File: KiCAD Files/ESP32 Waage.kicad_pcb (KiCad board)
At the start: 2 copper layers, 2 parts, among them J1 Conn_01x19_Female, U1 ESP32-WROVER

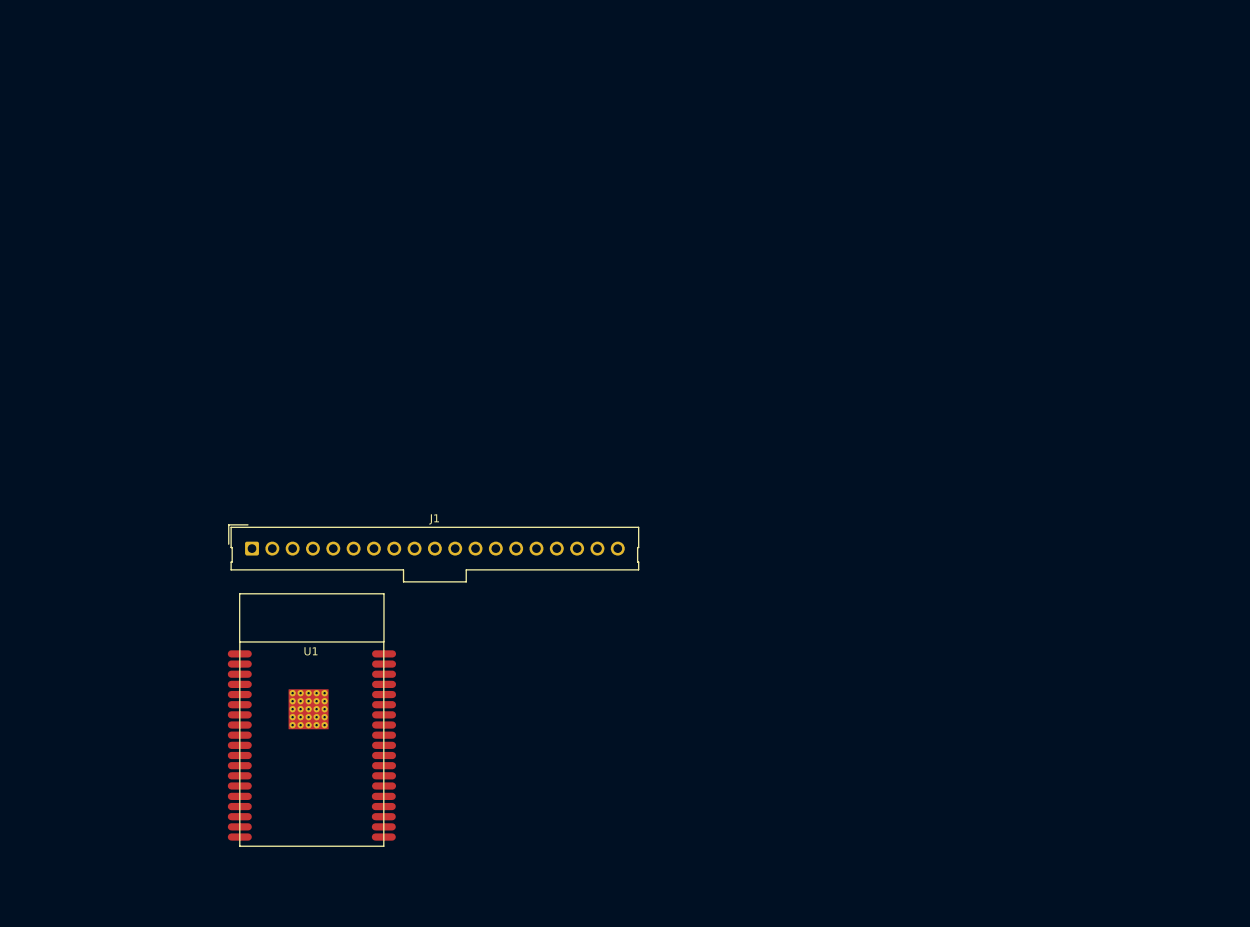
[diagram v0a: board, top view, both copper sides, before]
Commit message: Optocoupler Mounting holes
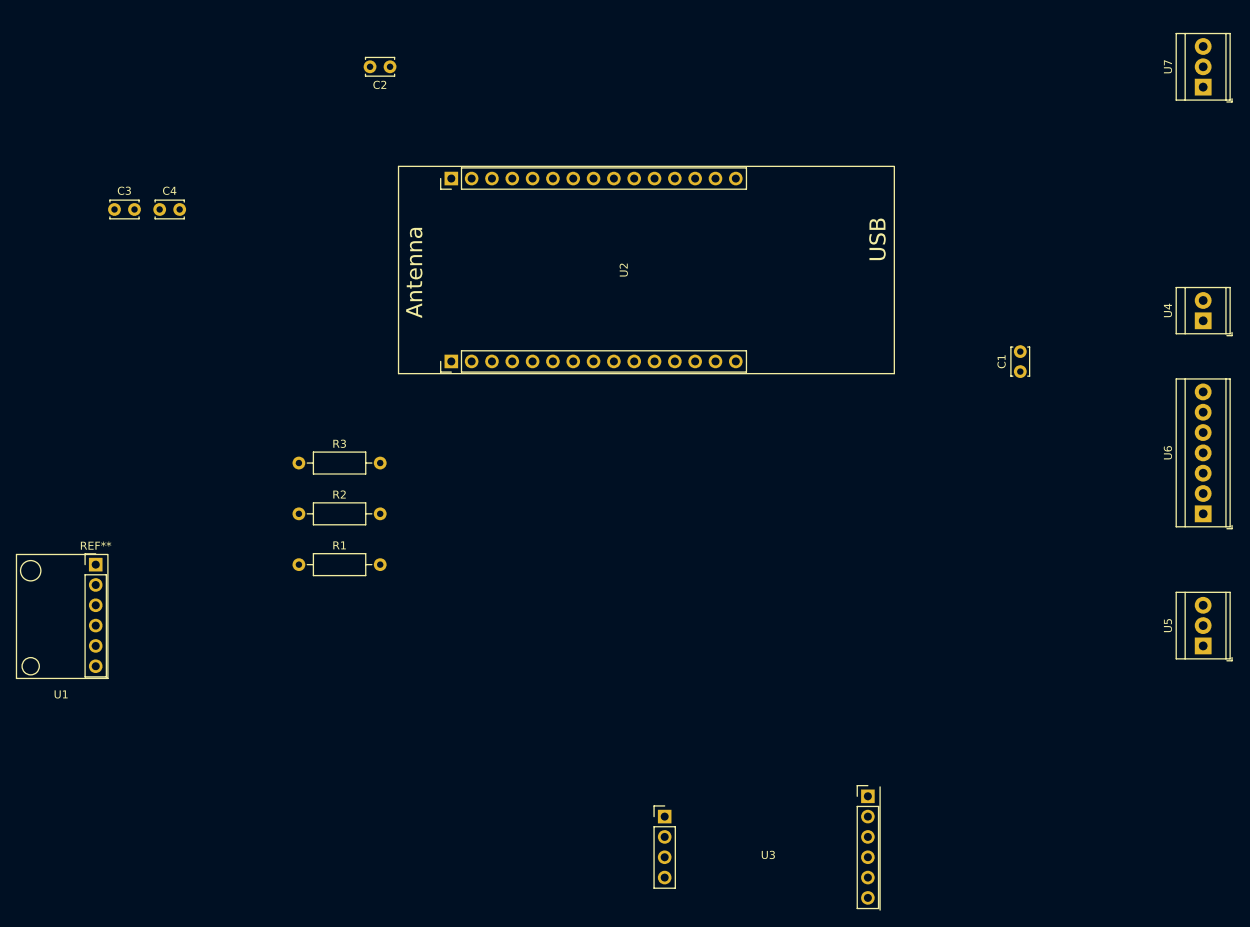
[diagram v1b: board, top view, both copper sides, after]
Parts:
- removed J1: Conn_01x19_Female, Connector_Molex:Molex_SL_171971-0019_1x19_P2.54mm_Vertical
- added C1: 47uF, Capacitor_THT:C_Disc_D3.4mm_W2.1mm_P2.50mm, F.Cu at (224.8, 61.0)
- added C2: 47uF, Capacitor_THT:C_Disc_D3.4mm_W2.1mm_P2.50mm, F.Cu at (146.0, 22.9)
- added C3: 1uF, Capacitor_THT:C_Disc_D3.4mm_W2.1mm_P2.50mm, F.Cu at (111.6, 40.7)
- added C4: 1uF, Capacitor_THT:C_Disc_D3.4mm_W2.1mm_P2.50mm, F.Cu at (117.2, 40.7)
- added R1: 4k7, Resistor_THT:R_Axial_DIN0207_L6.3mm_D2.5mm_P10.16mm_Horizontal, F.Cu at (134.6, 85.1)
- added R2: 4k7, Resistor_THT:R_Axial_DIN0207_L6.3mm_D2.5mm_P10.16mm_Horizontal, F.Cu at (134.6, 78.7)
- added R3: 4k7, Resistor_THT:R_Axial_DIN0207_L6.3mm_D2.5mm_P10.16mm_Horizontal, F.Cu at (134.6, 72.4)
- added U2: ESP32WROVERSocket, ESP32 Waage:TTGO_T8_Socket, F.Cu at (171.4, 48.3)
- added U3: HX711Socket, ESP32 Waage:HX711_Socket, F.Cu at (180.3, 120.7)
- added U4: SupplSpringTerm, TerminalBlock_TE-Connectivity:TerminalBlock_TE_282834-2_1x02_P2.54mm_Horizontal, F.Cu at (247.7, 54.6)
- added U5: DS18B20SpringTerm, TerminalBlock_TE-Connectivity:TerminalBlock_TE_282834-3_1x03_P2.54mm_Horizontal, F.Cu at (247.7, 95.2)
- added U6: HX711SpringTerm, TerminalBlock_TE-Connectivity:TerminalBlock_TE_282834-7_1x07_P2.54mm_Horizontal, F.Cu at (247.7, 78.7)
- added U7: I2SSpringTerm, TerminalBlock_TE-Connectivity:TerminalBlock_TE_282834-3_1x03_P2.54mm_Horizontal, F.Cu at (247.7, 25.4)
- U1: value ESP32-WROVER -> BME280Socket; footprint KiCadGlobalFootprint:ESP32-WROVER -> ESP32 Waage:BME280_Socket
- moved U1 27.3 mm to (109.2, 91.4)
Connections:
- U1 pad 5: Net-(U1-Pad5) -> GND

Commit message: added switch rearranged stuff
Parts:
- removed the C3 at (111.6, 40.7)
- removed the U3 at (180.3, 120.7)
- added C2: 47uF, Capacitor_SMD:C_0805_2012Metric_Pad1.15x1.40mm_HandSolder, F.Cu at (233.7, 21.3)
- added C5: 1uF, Capacitor_SMD:C_0805_2012Metric_Pad1.15x1.40mm_HandSolder, F.Cu at (236.5, 69.8)
- added SW1: SW_SPST, Button_Switch_THT:SW_CuK_JS202011CQN_DPDT_Straight, F.Cu at (241.3, 20.3)
- added TP1: TestPoint, TestPoint:TestPoint_THTPad_D2.0mm_Drill1.0mm, F.Cu at (204.5, 27.9)
- added TP10: TestPoint, TestPoint:TestPoint_THTPad_D2.0mm_Drill1.0mm, F.Cu at (224.8, 31.8)
- added TP11: TestPoint, TestPoint:TestPoint_THTPad_D2.0mm_Drill1.0mm, F.Cu at (194.3, 64.8)
- added TP12: TestPoint, TestPoint:TestPoint_THTPad_D2.0mm_Drill1.0mm, F.Cu at (199.4, 64.8)
- added TP13: TestPoint, TestPoint:TestPoint_THTPad_D2.0mm_Drill1.0mm, F.Cu at (204.5, 64.8)
- added TP14: TestPoint, TestPoint:TestPoint_THTPad_D2.0mm_Drill1.0mm, F.Cu at (212.1, 68.6)
- added TP15: TestPoint, TestPoint:TestPoint_THTPad_D2.0mm_Drill1.0mm, F.Cu at (196.8, 68.6)
- added TP16: TestPoint, TestPoint:TestPoint_THTPad_D2.0mm_Drill1.0mm, F.Cu at (201.9, 68.6)
- added TP17: TestPoint, TestPoint:TestPoint_THTPad_D2.0mm_Drill1.0mm, F.Cu at (214.6, 64.8)
- added TP2: TestPoint, TestPoint:TestPoint_THTPad_D2.0mm_Drill1.0mm, F.Cu at (209.6, 27.9)
- added TP3: TestPoint, TestPoint:TestPoint_THTPad_D2.0mm_Drill1.0mm, F.Cu at (214.6, 27.9)
- added TP4: TestPoint, TestPoint:TestPoint_THTPad_D2.0mm_Drill1.0mm, F.Cu at (219.7, 27.9)
- added TP5: TestPoint, TestPoint:TestPoint_THTPad_D2.0mm_Drill1.0mm, F.Cu at (227.3, 27.9)
- added TP6: TestPoint, TestPoint:TestPoint_THTPad_D2.0mm_Drill1.0mm, F.Cu at (201.9, 31.8)
- added TP7: TestPoint, TestPoint:TestPoint_THTPad_D2.0mm_Drill1.0mm, F.Cu at (207.0, 31.8)
- added TP8: TestPoint, TestPoint:TestPoint_THTPad_D2.0mm_Drill1.0mm, F.Cu at (212.1, 31.8)
- added TP9: TestPoint, TestPoint:TestPoint_THTPad_D2.0mm_Drill1.0mm, F.Cu at (217.2, 31.8)
- added U2: SN74LVC1T45DBV, Package_TO_SOT_SMD:SOT-23-6, F.Cu at (179.2, 34.0)
- added U7: DS18B20SpringTerm, TerminalBlock_TE-Connectivity:TerminalBlock_TE_282834-3_1x03_P2.54mm_Horizontal, F.Cu at (201.9, 81.3)
- added U9: I2CSpringTerm, TerminalBlock_TE-Connectivity:TerminalBlock_TE_282834-4_1x04_P2.54mm_Horizontal, F.Cu at (240.0, 81.3)
- C1: value 47uF -> 1uF; footprint Capacitor_THT:C_Disc_D3.4mm_W2.1mm_P2.50mm -> Capacitor_SMD:C_0805_2012Metric_Pad1.15x1.40mm_HandSolder
- C3: renamed from C2; footprint Capacitor_THT:C_Disc_D3.4mm_W2.1mm_P2.50mm -> Capacitor_SMD:C_0805_2012Metric_Pad1.15x1.40mm_HandSolder
- C4: footprint Capacitor_THT:C_Disc_D3.4mm_W2.1mm_P2.50mm -> Capacitor_SMD:C_0805_2012Metric_Pad1.15x1.40mm_HandSolder
- R1, R2, R3: footprint Resistor_THT:R_Axial_DIN0207_L6.3mm_D2.5mm_P10.16mm_Horizontal -> Resistor_SMD:R_0805_2012Metric_Pad1.15x1.40mm_HandSolder
- U1: value BME280Socket -> SupplSpringTerm; footprint ESP32 Waage:BME280_Socket -> TerminalBlock_TE-Connectivity:TerminalBlock_TE_282834-2_1x02_P2.54mm_Horizontal
- U4: value SupplSpringTerm -> HX711Socket; footprint TerminalBlock_TE-Connectivity:TerminalBlock_TE_282834-2_1x02_P2.54mm_Horizontal -> ESP32 Waage:HX711_Socket
- U5: value DS18B20SpringTerm -> BME280Socket; footprint TerminalBlock_TE-Connectivity:TerminalBlock_TE_282834-3_1x03_P2.54mm_Horizontal -> ESP32 Waage:BME280_Socket
- U8: renamed from U7; footprint TerminalBlock_TE-Connectivity:TerminalBlock_TE_282834-3_1x03_P2.54mm_Horizontal -> TerminalBlock_TE-Connectivity:TerminalBlock_TE_282834-6_1x06_P2.54mm_Horizontal
- moved U1 149.5 mm to (245.1, 29.2), turned to 270 degrees
- moved R3 100.5 mm to (234.9, 79.0), turned to 270 degrees
- moved R2 100.4 mm to (234.9, 82.8), turned to 90 degrees
- moved U4 74.5 mm to (174.0, 43.2), turned to 270 degrees
- moved R1 66.8 mm to (200.4, 73.7)
- moved U6 66.1 mm to (181.6, 81.3), turned to 180 degrees
- moved C4 59.9 mm to (176.8, 47.0)
- moved U8 58.6 mm to (229.9, 81.3), turned to 180 degrees
- moved C3 50.8 mm to (195.8, 33.0), turned to 0 degrees
- moved C1 41.6 mm to (237.5, 21.3), turned to 270 degrees
- moved U3 40.6 mm to (212.1, 48.3)
- moved U5 22.5 mm to (241.3, 73.7), turned to 270 degrees
- renumbered U2 to U3
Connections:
- C1 pad 1: GND -> +5V
- C1 pad 2: +5V -> GND
- C3 pad 2: Net-(C2-Pad2) -> +3V3
- R1 pad 1: Net-(C2-Pad2) -> Net-(R1-Pad1)
- R1 pad 2: Net-(R1-Pad2) -> +3V3
- R2 pad 1: Net-(C2-Pad2) -> Net-(R2-Pad1)
- R2 pad 2: Net-(R2-Pad2) -> +3V3
- R3 pad 1: GND -> Net-(R3-Pad1)
- R3 pad 2: Net-(C2-Pad2) -> +3V3
- U1 pad 2: Net-(U1-Pad2) -> GND
- U3 pad 12: Net-(U2-Pad12) -> Net-(U3-Pad12)
- U3 pad 13: Net-(U2-Pad13) -> Net-(R3-Pad1)
- U3 pad 14: Net-(U2-Pad14) -> Net-(U3-Pad14)
- U3 pad 15: Net-(U2-Pad15) -> Net-(R2-Pad1)
- U3 pad 18: Net-(U2-Pad18) -> Net-(TP3-Pad1)
- U3 pad 2: Net-(U2-Pad2) -> Net-(TP4-Pad1)
- U3 pad 27: Net-(U2-Pad27) -> Net-(U3-Pad27)
- U3 pad 32: Net-(R2-Pad2) -> Net-(U3-Pad32)
- U3 pad 33: Net-(R1-Pad2) -> Net-(R1-Pad1)
- U3 pad 3V3: (no net) -> +3V3
- U3 pad 5: Net-(U2-Pad5) -> Net-(TP9-Pad1)
- U4 pad 2: GND -> Net-(U3-Pad32)
- U5 pad 1: Net-(C2-Pad2) -> (no net)
- U5 pad 2: Net-(U2-Pad15) -> (no net)
- U5 pad 3: GND -> Net-(R2-Pad1)
- U6 pad 1: Net-(U3-Pad1) -> Net-(U4-Pad10)
- U6 pad 2: Net-(U3-Pad2) -> Net-(U4-Pad9)
- U6 pad 3: Net-(U3-Pad3) -> Net-(U4-Pad8)
- U6 pad 4: Net-(U3-Pad4) -> Net-(U4-Pad7)
- U6 pad 5: GND -> Net-(U4-Pad6)
- U6 pad 6: Net-(U3-Pad6) -> Net-(U4-Pad5)
- U8 pad 1: Net-(U2-Pad18) -> Net-(U3-Pad12)
- U8 pad 2: Net-(U2-Pad5) -> Net-(U3-Pad14)
- U8 pad 3: Net-(U2-Pad2) -> Net-(U3-Pad27)
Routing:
- net +3V3: track 0.00 -> 133.7 mm
- net +5V: track 0.00 -> 92.5 mm
- net Net-(R2-Pad1): track 0.00 -> 45.2 mm
- net Net-(U3-Pad32): track 0.00 -> 39.3 mm
- net Net-(R3-Pad1): track 0.00 -> 39.3 mm
- net Net-(R1-Pad1): track 0.00 -> 25.8 mm
- net Net-(U3-Pad27): track 0.00 -> 24.7 mm
- net Net-(U3-Pad14): track 0.00 -> 24.7 mm
- net Net-(U3-Pad12): track 0.00 -> 24.7 mm
- net GND: track 0.00 -> 24.5 mm, vias 0 -> 1
- net Net-(U2-Pad3): track 0.00 -> 23.5 mm
- net Net-(U4-Pad7): track 0.00 -> 13.1 mm
- net Net-(U4-Pad10): track 0.00 -> 13.1 mm
- net Net-(U4-Pad9): track 0.00 -> 13.1 mm
- net Net-(U4-Pad8): track 0.00 -> 13.1 mm
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- added copper zone on B.Cu, net GND
- added copper zone on F.Cu, net GND
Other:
- board text added: "A+"
- board text added: "A-"
- board text added: "B+"
- board text added: "B-"
- board text added: "E+"
- board text added: "E-"
- board text added: "SHD"

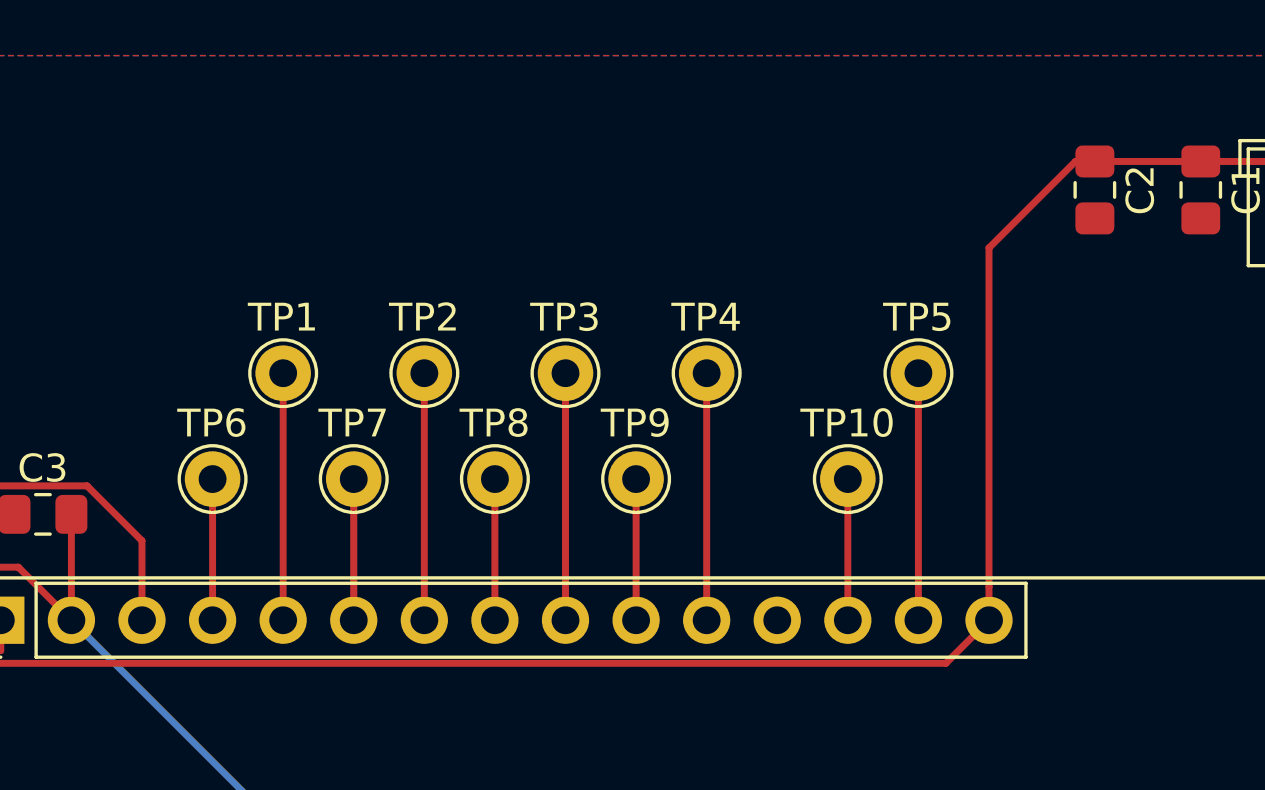
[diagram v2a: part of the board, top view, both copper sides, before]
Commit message: new schema layout
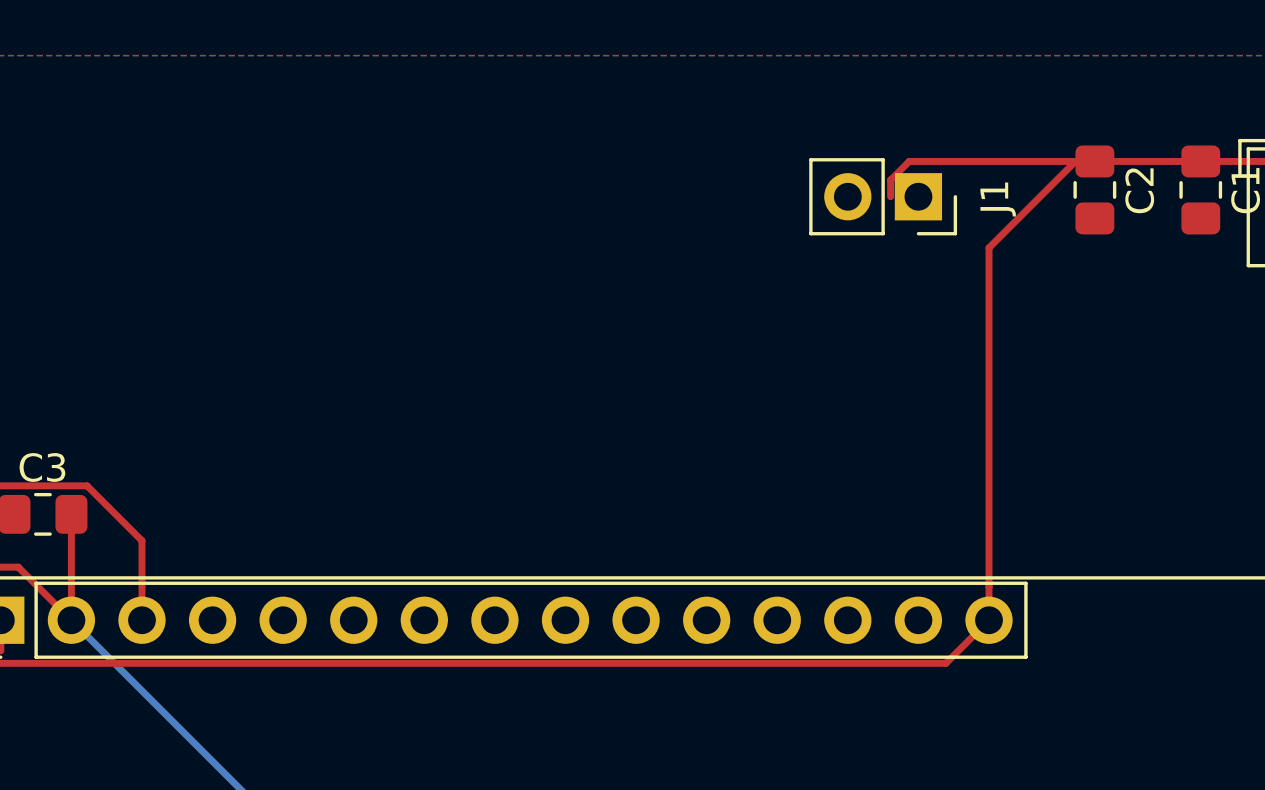
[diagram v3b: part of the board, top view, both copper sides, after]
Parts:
- removed TP1, TP10, TP2, TP3, TP4, TP5, TP6, TP7, TP8, TP9: TestPoint, TestPoint:TestPoint_THTPad_D2.0mm_Drill1.0mm
- added J1: 5V GND, Connector_PinSocket_2.54mm:PinSocket_1x02_P2.54mm_Vertical, F.Cu at (227.3, 21.6)
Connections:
- net Net-(U2-Pad3) renamed 21
- net Net-(U3-Pad32) renamed 32
- net Net-(U4-Pad10) renamed /B+
- U3 pad 0: Net-(TP10-Pad1) -> (no net)
- U3 pad 18: Net-(TP3-Pad1) -> (no net)
- U3 pad 19: Net-(TP2-Pad1) -> (no net)
- U3 pad 2: Net-(TP4-Pad1) -> (no net)
- U3 pad 22: Net-(TP7-Pad1) -> (no net)
- U3 pad 23: Net-(TP8-Pad1) -> (no net)
- U3 pad 4: Net-(TP5-Pad1) -> (no net)
- U3 pad 5: Net-(TP9-Pad1) -> (no net)
- U3 pad RXD: Net-(TP1-Pad1) -> (no net)
- U3 pad TXD: Net-(TP6-Pad1) -> (no net)
- U4 pad 6: Net-(U4-Pad6) -> GND
- U6 pad 5: Net-(U4-Pad6) -> GND
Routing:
- net Net-(U4-Pad6): track 13.1 -> 0.00 mm
- net GND: track 24.5 -> 37.6 mm
- net Net-(TP5-Pad1): track 8.89 -> 0.00 mm
- net Net-(TP4-Pad1): track 8.89 -> 0.00 mm
- net Net-(TP3-Pad1): track 8.89 -> 0.00 mm
- net Net-(TP2-Pad1): track 8.89 -> 0.00 mm
- net Net-(TP1-Pad1): track 8.89 -> 0.00 mm
- net +5V: track 92.5 -> 100.0 mm
- net Net-(TP9-Pad1): track 5.08 -> 0.00 mm
- net Net-(TP8-Pad1): track 5.08 -> 0.00 mm
- net Net-(TP7-Pad1): track 5.08 -> 0.00 mm
- net Net-(TP6-Pad1): track 5.08 -> 0.00 mm
- net Net-(TP10-Pad1): track 5.08 -> 0.00 mm

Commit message: redesign of schema added various 3D models PCB
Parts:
- removed TP11, TP12, TP13, TP14, TP15, TP16, TP17: TestPoint, TestPoint:TestPoint_THTPad_D2.0mm_Drill1.0mm
- removed U4: HX711Socket, ESP32 Waage:HX711_Socket
- removed U5: BME280Socket, ESP32 Waage:BME280_Socket
- removed U6: HX711SpringTerm, TerminalBlock_TE-Connectivity:TerminalBlock_TE_282834-7_1x07_P2.54mm_Horizontal
- removed U7: DS18B20SpringTerm, TerminalBlock_TE-Connectivity:TerminalBlock_TE_282834-3_1x03_P2.54mm_Horizontal
- removed U8: I2SSpringTerm, TerminalBlock_TE-Connectivity:TerminalBlock_TE_282834-6_1x06_P2.54mm_Horizontal
- removed U9: I2CSpringTerm, TerminalBlock_TE-Connectivity:TerminalBlock_TE_282834-4_1x04_P2.54mm_Horizontal
- added C6: 1uF, Capacitor_SMD:C_0805_2012Metric_Pad1.15x1.40mm_HandSolder, F.Cu at (198.6, 101.6)
- added J10: I2S Terminal, ESP32 Waage:PhoenixContact_FFKDSV_254_6_pol, F.Cu at (185.4, 113.7)
- added J11: Ext. BME280, ESP32 Waage:PhoenixContact_FFKDSV_254_6_pol, F.Cu at (219.1, 108.6)
- added J12: Int. BME280, ESP32 Waage:BME280_Socket, F.Cu at (197.5, 111.1)
- added J2: Ext. Power Supply 5V, ESP32 Waage:PhoenixContact_FFKDSV_254_2_pol, F.Cu at (218.8, 63.5)
- added J3: spare, Connector_PinHeader_2.54mm:PinHeader_1x08_P2.54mm_Vertical, F.Cu at (176.5, 69.2)
- added J4: spare, Connector_PinHeader_2.54mm:PinHeader_1x02_P2.54mm_Vertical, F.Cu at (199.4, 69.2)
- added J5: 5V spare, Connector_PinSocket_2.54mm:PinSocket_1x02_P2.54mm_Vertical, F.Cu at (185.9, 63.0)
- added J6: spare, Connector_PinHeader_2.54mm:PinHeader_1x05_P2.54mm_Vertical, F.Cu at (179.1, 102.2)
- added J7: spare, Connector_PinHeader_2.54mm:PinHeader_1x02_P2.54mm_Vertical, F.Cu at (189.2, 102.2)
- added J8: Scale Terminal, ESP32 Waage:PhoenixContact_FFKDSV_254_7_pol, F.Cu at (149.2, 113.7)
- added J9: DS18B20 Term., ESP32 Waage:PhoenixContact_FFKDSV_254_3_pol, F.Cu at (168.3, 113.7)
- C1: value 1uF -> 47uF
- C2: value 47uF -> 1uF
- J1: value 5V GND -> 3.3V spare
- U1: value SupplSpringTerm -> SN74LVC1T45DBV; footprint TerminalBlock_TE-Connectivity:TerminalBlock_TE_282834-2_1x02_P2.54mm_Horizontal -> Package_TO_SOT_SMD:SOT-23-6
- U2: value SN74LVC1T45DBV -> ESP32WROVERSocket; footprint Package_TO_SOT_SMD:SOT-23-6 -> ESP32 Waage:TTGO_T8_Socket
- U3: value ESP32WROVERSocket -> HX711Socket; footprint ESP32 Waage:TTGO_T8_Socket -> ESP32 Waage:HX711_Socket
- moved U1 88.1 mm to (164.5, 64.8), turned to 90 degrees
- moved R3 70.3 mm to (169.7, 105.2), turned to 0 degrees
- moved J1 68.5 mm to (172.7, 63.0)
- moved U3 65.8 mm to (148.6, 65.5), turned to 270 degrees
- moved C1 56.8 mm to (198.8, 62.9)
- moved SW1 56.6 mm to (202.6, 61.6)
- moved C2 55.9 mm to (196.2, 62.9)
- moved U2 52.3 mm to (186.7, 85.7), turned to 90 degrees
- moved C3 45.9 mm to (170.2, 71.1)
- moved C5 43.7 mm to (208.7, 103.5), turned to 270 degrees
- moved R2 41.2 mm to (206.2, 112.4), turned to 270 degrees
- moved R1 38.9 mm to (203.7, 112.4), turned to 270 degrees
- moved C4 37.5 mm to (148.6, 71.8)
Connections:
- C5 pad 1: GND -> +3V3
- C5 pad 2: +3V3 -> GND
- J1 pad 1: GND -> +3V3
- J1 pad 2: +5V -> GND
- R1 pad 1: Net-(R1-Pad1) -> SDC
- R2 pad 1: Net-(R2-Pad1) -> SDA
- R3 pad 1: Net-(R3-Pad1) -> GND
- R3 pad 2: +3V3 -> 33
- SW1 pad 2: Net-(SW1-Pad2) -> +5VL
- U1 pad 1: Net-(SW1-Pad2) -> (no net)
- U2 pad 2: GND -> Net-(J3-Pad8)
- U2 pad 5: GND -> Net-(J3-Pad7)
- U3 pad 2: (no net) -> 32
- U3 pad 4: (no net) -> GND
- U3 pad 5: (no net) -> Net-(J8-Pad2)
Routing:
- net SDA: track 0.00 -> 48.6 mm
- net Net-(R2-Pad1): track 45.2 -> 0.00 mm
- net Net-(R3-Pad1): track 39.3 -> 0.00 mm
- net SDC: track 0.00 -> 35.5 mm
- net 33: track 0.00 -> 26.4 mm
- net Net-(R1-Pad1): track 25.8 -> 0.00 mm
- net Net-(U3-Pad27): track 24.7 -> 0.00 mm
- net Net-(U3-Pad14): track 24.7 -> 0.00 mm
- net Net-(U3-Pad12): track 24.7 -> 0.00 mm
- net Net-(J8-Pad2): track 0.00 -> 21.4 mm
- net Net-(J8-Pad7): track 0.00 -> 21.3 mm
- net Net-(J8-Pad6): track 0.00 -> 21.3 mm
- net Net-(J8-Pad5): track 0.00 -> 21.3 mm
- net Net-(J8-Pad4): track 0.00 -> 21.3 mm
- net Net-(U1-Pad4): track 0.00 -> 20.0 mm
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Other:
- board outline added: 88.8 x 60.3 mm
- board text added: "3V3"
- board text added: "5V"
- board text added: "CSB"
- board text added: "DT"
- board text added: "GND"
- board text added: "LR"
- board text added: "OFF"
- board text added: "ON"
- board text added: "SCK"
- board text added: "SD"
- board text added: "SDA"
- board text added: "SDC"
- board text added: "SDO"
- board text added: "WS"
